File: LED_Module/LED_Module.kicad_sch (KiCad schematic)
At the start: 53 parts, among them J1 Conn_02x05_Odd_Even, J2 Conn_01x03_Male, J3 ESP8266 Header, J4 Barrel_Jack, SW1 SW_Push, SW2 SW_Push, U1 LD1117S33TR_SOT223, U2 STM32F091RCTx, U3 TPS62A02DRL, U4 24AA32AF EEPROM

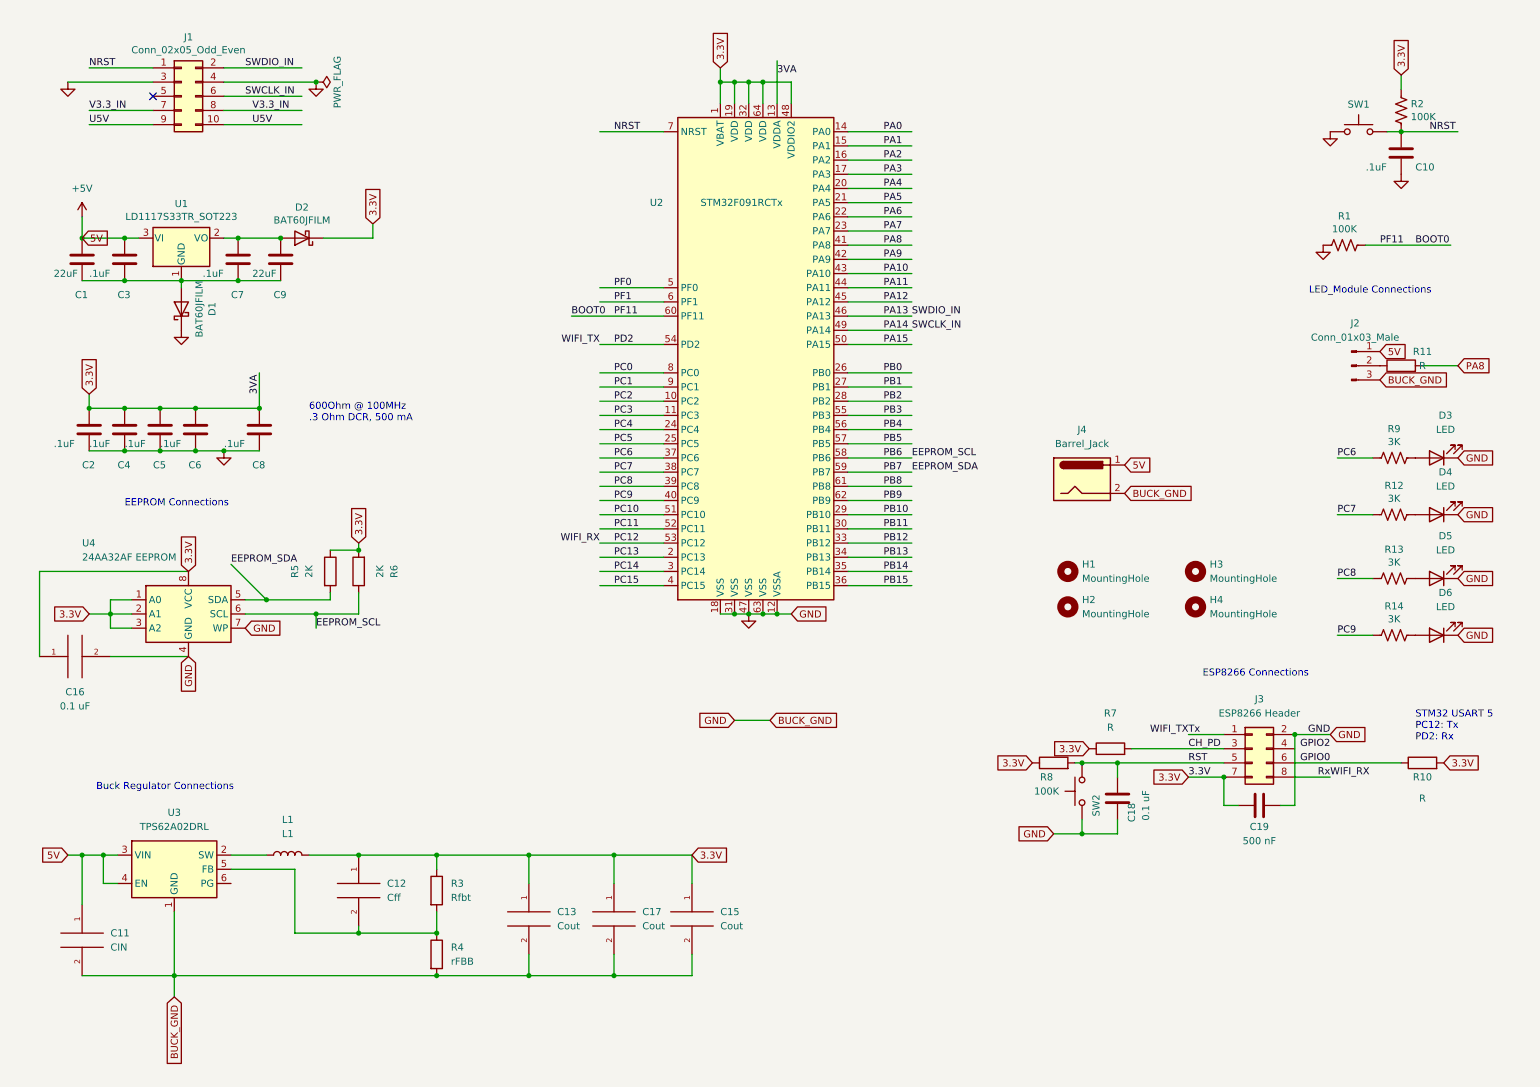
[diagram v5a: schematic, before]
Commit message: Added bulk capacitor, diode, and some extra vias
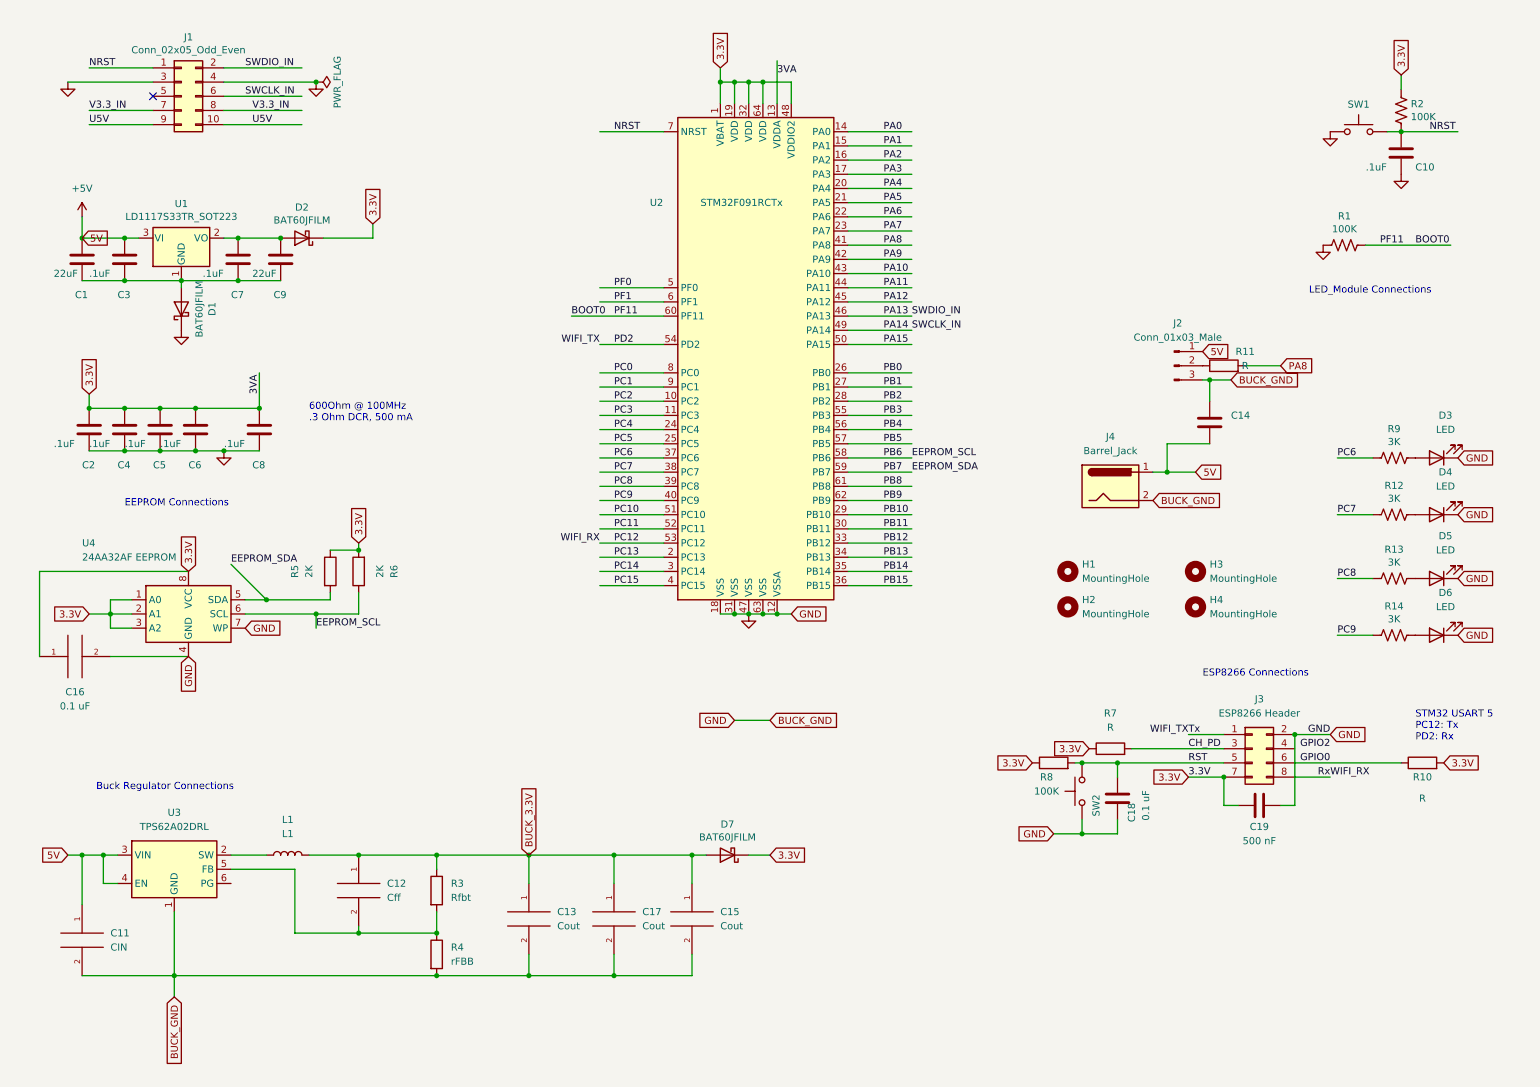
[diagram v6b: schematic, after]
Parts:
- added C14: (no value), symbol Device:C
- added D7: BAT60JFILM, Diode_SMD:D_SOD-323, symbol Diode:BAT60A
- D3, D4, D5, D6: footprint (none) -> LED_SMD:LED_0805_2012Metric_Pad1.15x1.40mm_HandSolder
- R12, R13, R14, R9: footprint (none) -> Resistor_SMD:R_0805_2012Metric_Pad1.20x1.40mm_HandSolder
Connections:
- net +5V: now also C14.2
- net 3.3V: now also D7.1 (K); no longer C12.1, C13.1, C15.1, C17.1, L1.2, R3.1
- net GND: now also C14.1
- new net BUCK_3.3V: C12.1, C13.1, C15.1, C17.1, D7.2 (A), L1.2, R3.1
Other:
- moved on the sheet: J2, J4, R11

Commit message: PCB design updated for week 8 design review
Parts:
- added D8, D9: LED, LED_SMD:LED_0805_2012Metric_Pad1.15x1.40mm_HandSolder, symbol Device:LED
- added R15, R16: 3K, Resistor_SMD:R_0805_2012Metric_Pad1.20x1.40mm_HandSolder, symbol Device:R_US
- C11, C13, C15, C17: footprint Capacitor_SMD:C_0805_2012Metric_Pad1.18x1.45mm_HandSolder -> (none)
- C12: footprint Capacitor_SMD:C_0402_1005Metric_Pad0.74x0.62mm_HandSolder -> (none)
- C14: value (none) -> 100uF; footprint (none) -> Capacitor_THT:C_Rect_L7.0mm_W2.0mm_P5.00mm
- L1: footprint Inductor_SMD:L_0603_1608Metric_Pad1.05x0.95mm_HandSolder -> (none)
- R3, R4: footprint Resistor_SMD:R_0805_2012Metric_Pad1.20x1.40mm_HandSolder -> (none)
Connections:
- net +5V: now also R15.2
- net 3.3V: now also R16.2
- net GND: now also D8.1 (K), D9.1 (K)
- new net: D9.2 (A), R16.1
- new net: D8.2 (A), R15.1
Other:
- note added: "5V Power and LED Grid"
- note added: "Boot0 Resistor"
- note added: "Buck Regulator"
- note added: "Debug and Power LEDs"
- note added: "Decoupling Capacitors"
- note added: "LDO (backup to Buck Converter)"
- note added: "Micro Reset Button"
- note added: "Mounting Holes"
- note added: "Program Header"
- note removed: "Buck Regulator Connections"
- note removed: "LED_Module Connections"
- moved on the sheet: C14, H1, H2, H3, H4, J2, J4, R11

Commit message: Final PCB Design used in order from PCB Way
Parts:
- C11: footprint (none) -> Capacitor_SMD:C_0805_2012Metric_Pad1.18x1.45mm_HandSolder
- C12: footprint (none) -> Capacitor_SMD:C_0402_1005Metric_Pad0.74x0.62mm_HandSolder
- C13, C15, C17: footprint (none) -> Capacitor_SMD:C_1206_3216Metric_Pad1.33x1.80mm_HandSolder
- C14: footprint Capacitor_THT:C_Rect_L7.0mm_W2.0mm_P5.00mm -> (none)
- J2: footprint Connector_JST:JST_PH_S3B-PH-K_1x03_P2.00mm_Horizontal -> (none)
- J4: footprint Connector_PinHeader_2.54mm:PinHeader_1x02_P2.54mm_Vertical -> (none)
- L1: footprint (none) -> Inductor_SMD:L_0603_1608Metric_Pad1.05x0.95mm_HandSolder
- R3, R4: footprint (none) -> Resistor_SMD:R_0805_2012Metric_Pad1.20x1.40mm_HandSolder
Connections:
- net U5V: no longer names the net of J1.10 (Pin_10)
- net U5V: no longer J1.9 (Pin_9)
- net V3.3_IN: no longer names the net of J1.7 (Pin_7)
- net V3.3_IN: no longer J1.8 (Pin_8)
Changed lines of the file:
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@@
-    (stroke (width 0) (type default) (color 0 0 0 0))
-  )
-  (wire (pts (xy 38.1 30.48) (xy 26.67 30.48))
     (stroke (width 0) (type default) (color 0 0 0 0))
   )
@@
     (stroke (width 0) (type default) (color 0 0 0 0))
   )
-  (wire (pts (xy 50.8 33.02) (xy 64.77 33.02))
-    (stroke (width 0) (type default) (color 0 0 0 0))
-  )
   (wire (pts (xy 105.41 168.91) (xy 105.41 163.83))
     (stroke (width 0) (type default) (color 0 0 0 0))
@@
     (stroke (width 0) (type default) (color 0 0 0 0))
   )
-  (wire (pts (xy 26.67 33.02) (xy 38.1 33.02))
-    (stroke (width 0) (type default) (color 0 0 0 0))
-  )
   (polyline (pts (xy 160.02 148.59) (xy 160.02 198.12))
     (stroke (width 0) (type default) (color 0 0 0 0))
@@
   )
   (wire (pts (xy 129.54 110.49) (xy 118.11 110.49))
-    (stroke (width 0) (type default) (color 0 0 0 0))
-  )
-  (wire (pts (xy 50.8 30.48) (xy 64.77 30.48))
     (stroke (width 0) (type default) (color 0 0 0 0))
   )
@@
     (effects (font (size 1.27 1.27)) (justify left bottom))
   )
-  (label "V3.3_IN" (at 55.88 30.48 0)
-    (effects (font (size 1.27 1.27)) (justify left bottom))
-  )
   (label "SWDIO_IN" (at 173.99 67.31 0)
     (effects (font (size 1.27 1.27)) (justify left bottom))
@@
     (effects (font (size 1.27 1.27)) (justify left bottom))
   )
-  (label "V3.3_IN" (at 26.67 30.48 0)
-    (effects (font (size 1.27 1.27)) (justify left bottom))
-  )
   (label "PA6" (at 168.91 49.53 0)
     (effects (font (size 1.27 1.27)) (justify left bottom))
@@
     (effects (font (size 1.27 1.27)) (justify left bottom))
   )
-  (label "U5V" (at 55.88 33.02 0)
-    (effects (font (size 1.27 1.27)) (justify left bottom))
-  )
   (label "PA2" (at 168.91 39.37 0)
     (effects (font (size 1.27 1.27)) (justify left bottom))
@@
   )
   (label "PC4" (at 120.65 87.63 0)
-    (effects (font (size 1.27 1.27)) (justify left bottom))
-  )
-  (label "U5V" (at 26.67 33.02 0)
     (effects (font (size 1.27 1.27)) (justify left bottom))
   )
@@
     (property "Reference" "L1" (id 0) (at 62.23 157.48 90))
     (property "Value" "L1" (id 1) (at 62.23 160.02 90))
-    (property "Footprint" "" (id 2) (at 62.23 163.83 0)
+    (property "Footprint" "Inductor_SMD:L_0603_1608Metric_Pad1.05x0.95mm_HandSolder" (id 2) (at 62.23 163.83 0)
       (effects (font (size 1.27 1.27)) hide)
     )
@@
       (effects (font (size 1.27 1.27)) (justify left))
     )
-    (property "Footprint" "" (id 2) (at 105.41 175.26 0)
+    (property "Footprint" "Capacitor_SMD:C_1206_3216Metric_Pad1.33x1.80mm_HandSolder" (id 2) (at 105.41 175.26 0)
       (effects (font (size 1.27 1.27)) hide)
     )
@@
     (property "Reference" "J2" (id 0) (at 216.535 17.78 0))
     (property "Value" "Conn_01x03_Male" (id 1) (at 216.535 20.32 0))
-    (property "Footprint" "Connector_JST:JST_PH_S3B-PH-K_1x03_P2.00mm_Horizontal" (id 2) (at 215.9 25.4 0)
+    (property "Footprint" "" (id 2) (at 215.9 25.4 0)
       (effects (font (size 1.27 1.27)) hide)
     )
@@
       (effects (font (size 1.27 1.27)) (justify left))
     )
-    (property "Footprint" "" (id 2) (at 74.93 170.18 0)
+    (property "Footprint" "Capacitor_SMD:C_0402_1005Metric_Pad0.74x0.62mm_HandSolder" (id 2) (at 74.93 170.18 0)
       (effects (font (size 1.27 1.27)) hide)
     )
@@
       (effects (font (size 1.27 1.27)) (justify left))
     )
-    (property "Footprint" "Capacitor_THT:C_Rect_L7.0mm_W2.0mm_P5.00mm" (id 2) (at 223.2152 39.37 0)
+    (property "Footprint" "" (id 2) (at 223.2152 39.37 0)
       (effects (font (size 1.27 1.27)) hide)
     )
@@
       (effects (font (size 1.27 1.27)) (justify left))
     )
-    (property "Footprint" "" (id 2) (at 25.4 179.07 0)
+    (property "Footprint" "Capacitor_SMD:C_0805_2012Metric_Pad1.18x1.45mm_HandSolder" (id 2) (at 25.4 179.07 0)
       (effects (font (size 1.27 1.27)) hide)
     )
@@
       (effects (font (size 1.27 1.27)) (justify left))
     )
-    (property "Footprint" "" (id 2) (at 87.122 181.61 90)
+    (property "Footprint" "Resistor_SMD:R_0805_2012Metric_Pad1.20x1.40mm_HandSolder" (id 2) (at 87.122 181.61 90)
       (effects (font (size 1.27 1.27)) hide)
     )
@@
       (effects (font (size 1.27 1.27)) (justify left))
     )
-    (property "Footprint" "" (id 2) (at 134.62 175.26 0)
+    (property "Footprint" "Capacitor_SMD:C_1206_3216Metric_Pad1.33x1.80mm_HandSolder" (id 2) (at 134.62 175.26 0)
       (effects (font (size 1.27 1.27)) hide)
     )
@@
       (effects (font (size 1.27 1.27)) (justify left))
     )
-    (property "Footprint" "" (id 2) (at 87.122 170.18 90)
+    (property "Footprint" "Resistor_SMD:R_0805_2012Metric_Pad1.20x1.40mm_HandSolder" (id 2) (at 87.122 170.18 90)
       (effects (font (size 1.27 1.27)) hide)
     )
@@
       (effects (font (size 1.27 1.27)) (justify left))
     )
-    (property "Footprint" "" (id 2) (at 120.65 175.26 0)
+    (property "Footprint" "Capacitor_SMD:C_1206_3216Metric_Pad1.33x1.80mm_HandSolder" (id 2) (at 120.65 175.26 0)
       (effects (font (size 1.27 1.27)) hide)
     )
@@
     (property "Reference" "J4" (id 0) (at 204.47 38.1 0))
     (property "Value" "Barrel_Jack" (id 1) (at 204.47 40.64 0))
-    (property "Footprint" "Connector_PinHeader_2.54mm:PinHeader_1x02_P2.54mm_Vertical" (id 2) (at 205.74 48.006 0)
+    (property "Footprint" "" (id 2) (at 205.74 48.006 0)
       (effects (font (size 1.27 1.27)) hide)
     )
@@
     )
     (path "/61a55e3a-73e1-4b5e-9e35-63f792c09229"
-      (reference "C14") (unit 1) (value "100uF") (footprint "Capacitor_THT:C_Rect_L7.0mm_W2.0mm_P5.00mm")
+      (reference "C14") (unit 1) (value "100uF") (footprint "Capacitor_THT:C_Radial_D10.0mm_H16.0mm_P5.00mm")
     )
     (path "/a2ce0818-68d2-4984-a143-7d29d5a77af4"
